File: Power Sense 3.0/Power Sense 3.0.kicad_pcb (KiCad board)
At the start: 2 copper layers, 133.9 x 50.3 mm, 49 parts, among them IC1 MCP3909, J1 Power, J2 ProgHead, J3 SPI, J4 TestHeader, T1 AC1030, T2 2p2sTransformer, U1 PIC18F25K20_I/SS, Y1 3.579545MHz Crystal

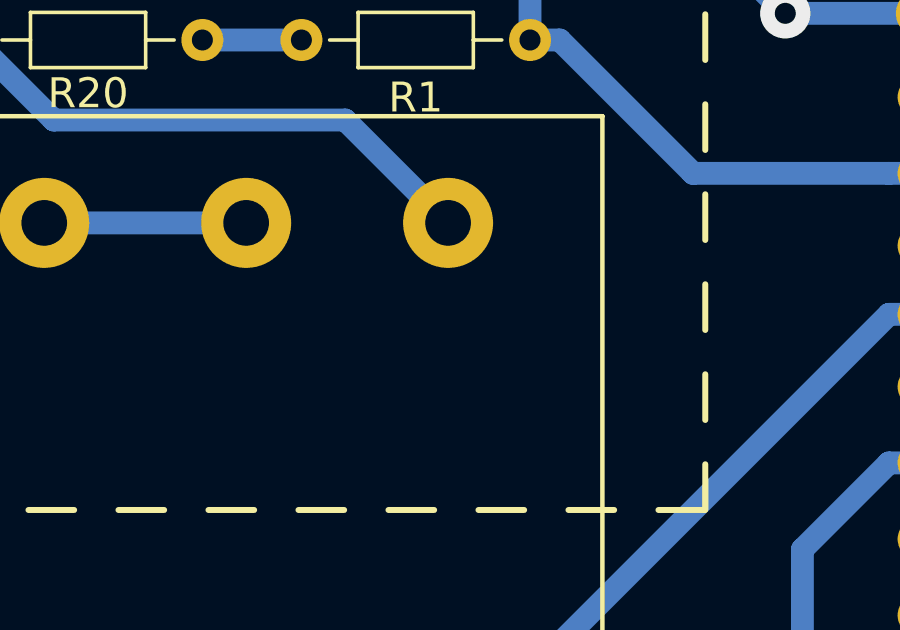
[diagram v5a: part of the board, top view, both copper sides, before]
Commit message: Added Pin 1 reference for transformer
Added "1" by pin 1 on transformer in both silkscreen and coppe
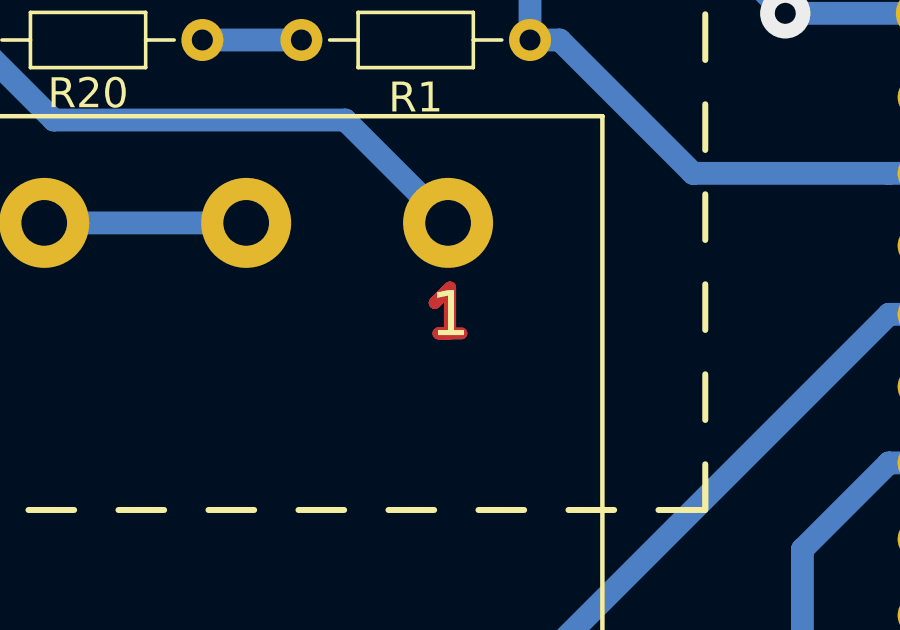
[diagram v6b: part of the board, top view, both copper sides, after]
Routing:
- net (no net): track 4.87 -> 9.70 mm, vias 0 -> 1
- net GND: track 296.5 -> 295.8 mm, vias 8 -> 7
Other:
- board text added: "1"
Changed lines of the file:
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@@
-(kicad_pcb (version 20171130) (host pcbnew "(5.0.0)")
+(kicad_pcb (version 4) (host pcbnew 4.0.7)
   (general
+    (links 102)
+    (no_connects 1)
+    (area -0.075001 -0.075001 201.092486 105.2652)
     (thickness 1.6)
-    (drawings 69)
-    (tracks 463)
+    (drawings 70)
+    (tracks 468)
     (zones 0)
     (modules 49)
@@
   )
   (setup
-    (last_trace_width 0.762)
+    (last_trace_width 0.4064)
     (user_trace_width 0.4064)
     (user_trace_width 0.762)
@@
       (layerselection 0x00030_80000001)
       (usegerberextensions false)
-      (usegerberattributes false)
-      (usegerberadvancedattributes false)
-      (creategerberjobfile false)
       (excludeedgelayer true)
       (linewidth 0.100000)
@@
       (hpglpennumber 1)
       (hpglpenspeed 20)
-      (hpglpendiameter 15.000000)
+      (hpglpendiameter 15)
+      (hpglpenoverlay 2)
       (psnegative false)
       (psa4output false)
@@
     (fp_line (start 3.55 1.15) (end 3.55 -1.15) (layer F.CrtYd) (width 0.05))
     (fp_line (start 3.55 -1.15) (end -1.05 -1.15) (layer F.CrtYd) (width 0.05))
-    (fp_text user %R (at 1.0795 0.0635 90) (layer F.Fab)
+    (fp_text user %R (at 1.0795 0.0635 450) (layer F.Fab)
       (effects (font (size 1 1) (thickness 0.15)))
     )
@@
     (fp_line (start 1.8 4.35) (end 1.8 -1.8) (layer F.CrtYd) (width 0.05))
     (fp_line (start 1.8 -1.8) (end -1.8 -1.8) (layer F.CrtYd) (width 0.05))
-    (fp_text user %R (at 0.254 1.27 90) (layer F.Fab)
+    (fp_text user %R (at 0.254 1.27 450) (layer F.Fab)
       (effects (font (size 1 1) (thickness 0.15)))
     )
@@
       (effects (font (size 1 1) (thickness 0.15)))
     )
-    (fp_text value PIC18F25K20_I/SS (at 4.064 18.034 90) (layer F.Fab)
+    (fp_text value PIC18F25K20_I/SS (at 4.064 18.034 450) (layer F.Fab)
       (effects (font (size 1 1) (thickness 0.15)))
     )
@@
       (effects (font (size 1 1) (thickness 0.15)))
     )
-    (fp_text user %R (at 0 6.35) (layer F.Fab)
+    (fp_text user %R (at 0 6.35 360) (layer F.Fab)
       (effects (font (size 1 1) (thickness 0.15)))
     )
@@
     )
     (pad 1 np_thru_hole circle (at 0 0) (size 4 4) (drill 4) (layers *.Cu *.Mask))
+  )
+  (gr_text 1 (at 99.06 68.707) (layer F.SilkS)
+    (effects (font (size 1.5 1.5) (thickness 0.3)))
   )
   (gr_poly (pts (xy 159.5755 98.679) (xy 160.5915 97.663) (xy 160.5915 98.3615) (xy 162.1155 98.3615) (xy 162.1155 98.9965) (xy 160.5915 98.9965) (xy 160.5915 99.695)) (layer F.SilkS) (width 0.15))
@@
   (segment (start 169.6085 80.264) (end 167.0685 80.264) (width 0.762) (layer F.Cu) (net 0))
   (segment (start 167.0685 80.264) (end 167.8305 79.502) (width 0.762) (layer F.Cu) (net 0))
+  (segment (start 162.4965 98.679) (end 161.8615 98.679) (width 0.762) (layer F.Cu) (net 0))
+  (segment (start 161.8615 98.679) (end 159.8295 98.679) (width 0.762) (layer F.Cu) (net 0))
+  (via (at 105.918 100.584) (size 1.6764) (drill 0.7) (layers F.Cu B.Cu) (net 0))
+  (segment (start 159.8295 98.679) (end 160.5915 99.441) (width 0.762) (layer F.Cu) (net 0))
+  (segment (start 159.8295 98.679) (end 160.5915 97.917) (width 0.762) (layer F.Cu) (net 0))
+  (segment (start 99.06 67.818) (end 98.552 68.326) (width 0.4064) (layer F.Cu) (net 1))
+  (segment (start 99.441 69.342) (end 98.679 69.342) (width 0.4064) (layer F.Cu) (net 1))
+  (segment (start 99.06 69.342) (end 98.679 69.342) (width 0.4064) (layer F.Cu) (net 1))
+  (segment (start 99.06 67.818) (end 99.06 69.342) (width 0.4064) (layer F.Cu) (net 1))
+  (segment (start 98.552 68.326) (end 99.06 67.818) (width 0.4064) (layer F.Cu) (net 1))
   (via (at 118.9355 81.661) (size 1.6764) (drill 0.7) (layers F.Cu B.Cu) (net 1))
-  (via (at 142.3035 94.8055) (size 1.6764) (drill 0.7) (layers F.Cu B.Cu) (net 5))
-  (via (at 142.875 86.995) (size 1.6764) (drill 0.7) (layers F.Cu B.Cu) (net 21))
-  (via (at 139.446 89.0905) (size 1.6764) (drill 0.7) (layers F.Cu B.Cu) (net 20))
-  (segment (start 162.4965 98.679) (end 161.8615 98.679) (width 0.762) (layer F.Cu) (net 1))
-  (segment (start 161.8615 98.679) (end 159.8295 98.679) (width 0.762) (layer F.Cu) (net 1))
   (via (at 110.236 58.674) (size 1.6764) (drill 0.7) (layers F.Cu B.Cu) (net 1))
   (segment (start 153.67 74.89) (end 154.519 74.89) (width 0.762) (layer B.Cu) (net 1) (status 10))
@@
   (segment (start 94.1578 56.9722) (end 94.234 56.896) (width 0.762) (layer B.Cu) (net 1) (status 30))
   (segment (start 110.236 58.674) (end 114.721 58.674) (width 0.762) (layer B.Cu) (net 1) (status 20))
-  (segment (start 131.318 80.137) (end 131.318 80.137) (width 0.762) (layer B.Cu) (net 50))
-  (segment (start 135.6995 79.080002) (end 133.517998 79.080002) (width 0.4064) (layer B.Cu) (net 50) (status 10))
-  (segment (start 133.517998 79.080002) (end 132.461 80.137) (width 0.4064) (layer B.Cu) (net 50))
-  (segment (start 135.6995 78.430001) (end 131.627999 78.430001) (width 0.4064) (layer B.Cu) (net 2) (status 10))
   (segment (start 122.468 66.421) (end 124.841 68.794) (width 0.762) (layer B.Cu) (net 1) (status 30))
   (segment (start 122.301 66.421) (end 122.468 66.421) (width 0.762) (layer B.Cu) (net 1) (status 30))
@@
   (segment (start 118.9355 81.661) (end 122.301 81.661) (width 0.762) (layer B.Cu) (net 1))
   (segment (start 110.6805 100.584) (end 126.492 100.584) (width 0.762) (layer B.Cu) (net 1))
-  (via (at 105.918 100.584) (size 1.6764) (drill 0.7) (layers F.Cu B.Cu) (net 1))
+  (segment (start 135.6995 78.430001) (end 131.627999 78.430001) (width 0.4064) (layer B.Cu) (net 2) (status 10))
   (segment (start 122.301 71.12) (end 124.841 71.12) (width 0.762) (layer B.Cu) (net 2) (status 30))
   (segment (start 124.841 71.12) (end 126.873 73.152) (width 0.762) (layer B.Cu) (net 2))
@@
   (segment (start 131.953 73.533) (end 132.969 74.549) (width 0.762) (layer B.Cu) (net 4))
   (segment (start 131.953 72.898) (end 131.953 73.533) (width 0.762) (layer B.Cu) (net 4))
+  (via (at 142.3035 94.8055) (size 1.6764) (drill 0.7) (layers F.Cu B.Cu) (net 5))
   (segment (start 135.6995 81.03) (end 135.6995 80.380002) (width 0.4064) (layer B.Cu) (net 5) (status 30))
   (segment (start 135.6995 81.679999) (end 135.6995 81.03) (width 0.4064) (layer B.Cu) (net 5) (status 30))
@@
   (segment (start 138.811 68.326) (end 140.335 66.802) (width 0.762) (layer F.Cu) (net 19))
   (segment (start 138.811 71.628) (end 138.811 68.326) (width 0.762) (layer F.Cu) (net 19))
+  (via (at 139.446 89.0905) (size 1.6764) (drill 0.7) (layers F.Cu B.Cu) (net 20))
   (segment (start 146.292999 80.379999) (end 148.59 82.677) (width 0.762) (layer B.Cu) (net 20))
   (segment (start 142.9385 80.379999) (end 146.292999 80.379999) (width 0.4064) (layer B.Cu) (net 20) (status 10))
@@
   (segment (start 134.112 94.4245) (end 139.446 89.0905) (width 0.762) (layer B.Cu) (net 20))
   (segment (start 134.112 100.584) (end 134.112 94.4245) (width 0.762) (layer B.Cu) (net 20))
+  (via (at 142.875 86.995) (size 1.6764) (drill 0.7) (layers F.Cu B.Cu) (net 21))
   (segment (start 145.415 81.788) (end 145.415 83.185) (width 0.762) (layer B.Cu) (net 21))
   (segment (start 168.021 83.058) (end 146.558 83.058) (width 0.762) (layer F.Cu) (net 21))
@@
   (segment (start 157.861 101.473) (end 144.018 101.473) (width 0.762) (layer B.Cu) (net 24))
   (segment (start 144.018 101.473) (end 143.129 100.584) (width 0.762) (layer B.Cu) (net 24))
-  (segment (start 159.8295 98.679) (end 160.5915 99.441) (width 0.762) (layer F.Cu) (net 1))
-  (segment (start 159.8295 98.679) (end 160.5915 97.917) (width 0.762) (layer F.Cu) (net 1))
   (segment (start 173.863 91.059) (end 174.498 90.424) (width 0.762) (layer B.Cu) (net 25) (status 30))
   (segment (start 157.353 91.059) (end 173.863 91.059) (width 0.762) (layer B.Cu) (net 25) (status 30))
@@
   (segment (start 182.753 62.484) (end 184.912 60.325) (width 0.762) (layer B.Cu) (net 42) (status 10))
   (segment (start 182.118 62.484) (end 182.753 62.484) (width 0.762) (layer B.Cu) (net 42) (status 30))
+  (segment (start 131.318 80.137) (end 131.318 80.137) (width 0.762) (layer B.Cu) (net 50))
+  (segment (start 135.6995 79.080002) (end 133.517998 79.080002) (width 0.4064) (layer B.Cu) (net 50) (status 10))
+  (segment (start 133.517998 79.080002) (end 132.461 80.137) (width 0.4064) (layer B.Cu) (net 50))
   (segment (start 131.318 80.137) (end 132.461 80.137) (width 0.762) (layer B.Cu) (net 50))
   (segment (start 128.397 80.137) (end 131.318 80.137) (width 0.762) (layer B.Cu) (net 50))

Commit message: First round of edits
Edited things in README.txt
See that file for changes
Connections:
- C3 pad 2: Net-(C3-Pad2) -> /CH1-
- IC1 pad 7: Net-(C3-Pad2) -> /CH1-
- J4 pad 4: /CH1+ -> /CH1-
- R8 pad 2: Net-(C3-Pad2) -> /CH1-
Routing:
- net /CH1-: track 0.00 -> 52.6 mm
- net /CH1+: track 58.3 -> 29.7 mm
- net Net-(C3-Pad2): track 22.3 -> 0.00 mm
- net GND: track 295.8 -> 300.6 mm, vias 7 -> 8
- net (no net): track 9.70 -> 4.87 mm, vias 1 -> 0

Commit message: Changed Transformer Resistor Divider R value
Changed 10k to 20k for 240v use
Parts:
- R5: value 10k 1% -> 20k 1%
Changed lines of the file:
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@@
   )
   (setup
-    (last_trace_width 0.4064)
+    (last_trace_width 0.762)
     (user_trace_width 0.4064)
     (user_trace_width 0.762)
@@
       (effects (font (size 1 1) (thickness 0.15)))
     )
-    (fp_text value "10k 1%" (at 3.81 1.86 180) (layer F.Fab)
+    (fp_text value "20k 1%" (at 3.81 1.86 180) (layer F.Fab)
       (effects (font (size 1 1) (thickness 0.15)))
     )
@@
   (segment (start 126.873 75.648617) (end 128.193801 76.969418) (width 0.762) (layer B.Cu) (net 2))
   (segment (start 126.873 73.152) (end 126.873 75.648617) (width 0.762) (layer B.Cu) (net 2))
-  (segment (start 133.025002 77.780002) (end 132.334 77.089) (width 0.4064) (layer B.Cu) (net 56))
-  (segment (start 133.533002 77.780002) (end 135.6995 77.780002) (width 0.4064) (layer B.Cu) (net 56) (status 20))
-  (segment (start 133.533002 77.780002) (end 133.025002 77.780002) (width 0.4064) (layer B.Cu) (net 56))
-  (segment (start 122.555 64.008) (end 124.841 66.294) (width 0.762) (layer B.Cu) (net 56) (status 30))
-  (segment (start 122.301 64.008) (end 122.555 64.008) (width 0.762) (layer B.Cu) (net 56) (status 30))
-  (segment (start 127 68.453) (end 124.841 66.294) (width 0.762) (layer B.Cu) (net 56))
-  (segment (start 127 71.596013) (end 127 68.453) (width 0.762) (layer B.Cu) (net 56))
-  (segment (start 128.397 72.993013) (end 127 71.596013) (width 0.762) (layer B.Cu) (net 56))
-  (segment (start 128.397 75.311) (end 128.397 72.993013) (width 0.762) (layer B.Cu) (net 56))
-  (segment (start 132.334 77.089) (end 130.175 77.089) (width 0.762) (layer B.Cu) (net 56))
-  (segment (start 130.175 77.089) (end 128.397 75.311) (width 0.762) (layer B.Cu) (net 56))
   (segment (start 134.250001 75.830001) (end 132.969 74.549) (width 0.4064) (layer B.Cu) (net 3))
   (segment (start 134.250001 75.830001) (end 135.6995 75.830001) (width 0.4064) (layer B.Cu) (net 3) (status 20))
@@
   (segment (start 131.318 75.819) (end 132.588 75.819) (width 0.762) (layer B.Cu) (net 50))
   (segment (start 130.048 74.549) (end 131.318 75.819) (width 0.762) (layer B.Cu) (net 50))
-  (segment (start 139.0015 83.312) (end 139.0015 86.0425) (width 0.762) (layer B.Cu) (net 56))
-  (segment (start 131.572 93.472) (end 131.572 100.584) (width 0.762) (layer B.Cu) (net 56))
   (segment (start 119.507 58.674) (end 122.301 61.468) (width 0.762) (layer B.Cu) (net 50))
   (segment (start 117.221 58.674) (end 119.507 58.674) (width 0.762) (layer B.Cu) (net 50))
-  (segment (start 139.0015 86.0425) (end 131.572 93.472) (width 0.762) (layer B.Cu) (net 56))
   (segment (start 85.5345 65.659) (end 92.2655 65.659) (width 0.762) (layer B.Cu) (net 51))
   (segment (start 83.1342 56.9722) (end 83.185 57.023) (width 0.762) (layer B.Cu) (net 54))
@@
   (segment (start 73.6473 56.9722) (end 71.9455 58.674) (width 0.762) (layer B.Cu) (net 54))
   (segment (start 90.805 59.563) (end 94.107 59.563) (width 0.762) (layer B.Cu) (net 55))
+  (segment (start 133.025002 77.780002) (end 132.334 77.089) (width 0.4064) (layer B.Cu) (net 56))
+  (segment (start 133.533002 77.780002) (end 135.6995 77.780002) (width 0.4064) (layer B.Cu) (net 56) (status 20))
+  (segment (start 133.533002 77.780002) (end 133.025002 77.780002) (width 0.4064) (layer B.Cu) (net 56))
+  (segment (start 122.555 64.008) (end 124.841 66.294) (width 0.762) (layer B.Cu) (net 56) (status 30))
+  (segment (start 122.301 64.008) (end 122.555 64.008) (width 0.762) (layer B.Cu) (net 56) (status 30))
+  (segment (start 127 68.453) (end 124.841 66.294) (width 0.762) (layer B.Cu) (net 56))
+  (segment (start 127 71.596013) (end 127 68.453) (width 0.762) (layer B.Cu) (net 56))
+  (segment (start 128.397 72.993013) (end 127 71.596013) (width 0.762) (layer B.Cu) (net 56))
+  (segment (start 128.397 75.311) (end 128.397 72.993013) (width 0.762) (layer B.Cu) (net 56))
+  (segment (start 132.334 77.089) (end 130.175 77.089) (width 0.762) (layer B.Cu) (net 56))
+  (segment (start 130.175 77.089) (end 128.397 75.311) (width 0.762) (layer B.Cu) (net 56))
+  (segment (start 139.0015 83.312) (end 139.0015 86.0425) (width 0.762) (layer B.Cu) (net 56))
+  (segment (start 131.572 93.472) (end 131.572 100.584) (width 0.762) (layer B.Cu) (net 56))
+  (segment (start 139.0015 86.0425) (end 131.572 93.472) (width 0.762) (layer B.Cu) (net 56))
   (segment (start 137.215993 77.786411) (end 136.912952 77.786411) (width 0.4064) (layer B.Cu) (net 56))
   (segment (start 139.0015 79.571918) (end 137.215993 77.786411) (width 0.4064) (layer B.Cu) (net 56))
